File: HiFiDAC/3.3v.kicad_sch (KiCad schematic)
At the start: 7 parts, among them U1 TPS7A90

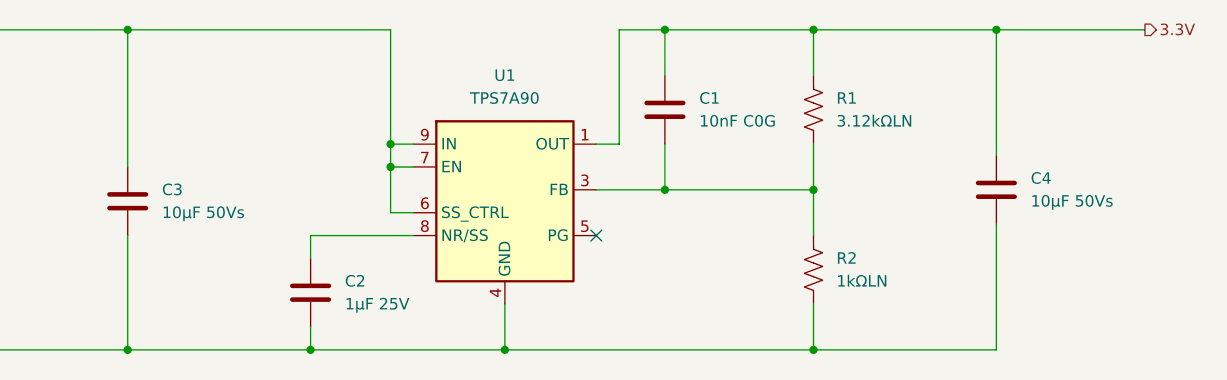
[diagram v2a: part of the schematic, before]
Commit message: HiFiDAC renumbered and footprints assigned
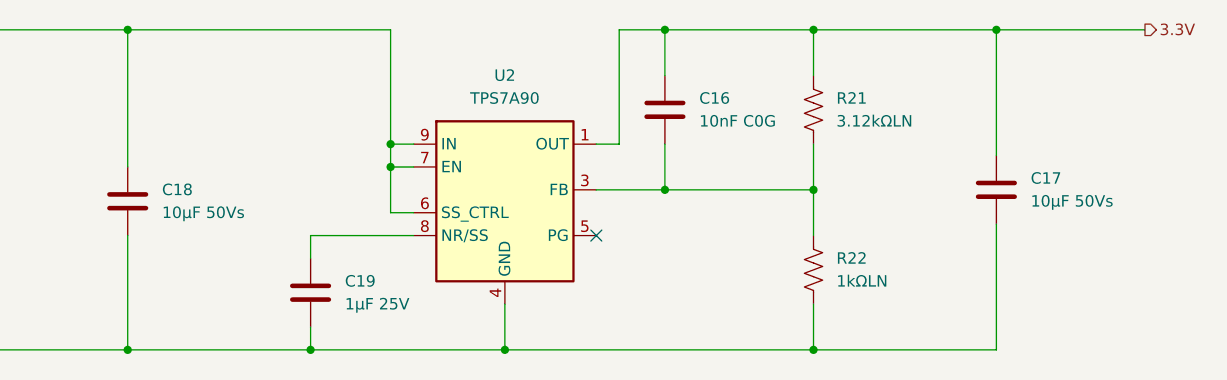
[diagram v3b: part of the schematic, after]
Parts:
- C16: renamed from C1; footprint (none) -> Capacitor_SMD:C_0603_1608Metric
- C17: renamed from C4; footprint (none) -> Capacitor_SMD:C_0805_2012Metric
- C18: renamed from C3; footprint (none) -> Capacitor_SMD:C_0805_2012Metric
- C19: renamed from C2; footprint (none) -> Capacitor_SMD:C_0603_1608Metric
- R21: renamed from R1; footprint (none) -> Resistor_SMD:R_0603_1608Metric
- R22: renamed from R2; footprint (none) -> Resistor_SMD:R_0603_1608Metric
- renumbered U1 to U2
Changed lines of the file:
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@@
 		(dnp no)
 		(fields_autoplaced yes)
-		(property "Reference" "R1"
+		(property "Reference" "R21"
 			(at 180.34 88.8999 0)
 			(effects
@@
 			)
 		)
-		(property "Footprint" ""
+		(property "Footprint" "Resistor_SMD:R_0603_1608Metric"
 			(at 178.816 90.424 90)
 			(effects
@@
 			(project ""
 				(path "/9ca5e549-4577-422c-b8f3-d4e6ad408ec3/d2b42ea6-55ff-4972-b433-f15f9f1c7608"
-					(reference "R1")
+					(reference "R21")
 					(unit 1)
 				)
@@
 		(dnp no)
 		(fields_autoplaced yes)
-		(property "Reference" "C3"
+		(property "Reference" "C18"
 			(at 105.41 99.0599 0)
 			(effects
@@
 			)
 		)
-		(property "Footprint" ""
+		(property "Footprint" "Capacitor_SMD:C_0805_2012Metric"
 			(at 102.5652 104.14 0)
 			(effects
@@
 			(project "HiFiDAC"
 				(path "/9ca5e549-4577-422c-b8f3-d4e6ad408ec3/d2b42ea6-55ff-4972-b433-f15f9f1c7608"
-					(reference "C3")
+					(reference "C18")
 					(unit 1)
 				)
@@
 		(dnp no)
 		(fields_autoplaced yes)
-		(property "Reference" "C4"
+		(property "Reference" "C17"
 			(at 201.93 97.7899 0)
 			(effects
@@
 			)
 		)
-		(property "Footprint" ""
+		(property "Footprint" "Capacitor_SMD:C_0805_2012Metric"
 			(at 199.0852 102.87 0)
 			(effects
@@
 			(project "HiFiDAC"
 				(path "/9ca5e549-4577-422c-b8f3-d4e6ad408ec3/d2b42ea6-55ff-4972-b433-f15f9f1c7608"
-					(reference "C4")
+					(reference "C17")
 					(unit 1)
 				)
@@
 		(dnp no)
 		(fields_autoplaced yes)
-		(property "Reference" "R2"
+		(property "Reference" "R22"
 			(at 180.34 106.6799 0)
 			(effects
@@
 			)
 		)
-		(property "Footprint" ""
+		(property "Footprint" "Resistor_SMD:R_0603_1608Metric"
 			(at 178.816 108.204 90)
 			(effects
@@
 			(project "HiFiDAC"
 				(path "/9ca5e549-4577-422c-b8f3-d4e6ad408ec3/d2b42ea6-55ff-4972-b433-f15f9f1c7608"
-					(reference "R2")
+					(reference "R22")
 					(unit 1)
 				)
@@
 		(dnp no)
 		(fields_autoplaced yes)
-		(property "Reference" "C2"
+		(property "Reference" "C19"
 			(at 125.73 109.2199 0)
 			(effects
@@
 			)
 		)
-		(property "Footprint" ""
+		(property "Footprint" "Capacitor_SMD:C_0603_1608Metric"
 			(at 122.8852 114.3 0)
 			(effects
@@
 			(project "HiFiDAC"
 				(path "/9ca5e549-4577-422c-b8f3-d4e6ad408ec3/d2b42ea6-55ff-4972-b433-f15f9f1c7608"
-					(reference "C2")
+					(reference "C19")
 					(unit 1)
 				)
@@
 		(dnp no)
 		(fields_autoplaced yes)
-		(property "Reference" "C1"
+		(property "Reference" "C16"
 			(at 165.1 88.8999 0)
 			(effects
@@
 			)
 		)
-		(property "Footprint" ""
+		(property "Footprint" "Capacitor_SMD:C_0603_1608Metric"
 			(at 162.2552 93.98 0)
 			(effects
@@
 			(project ""
 				(path "/9ca5e549-4577-422c-b8f3-d4e6ad408ec3/d2b42ea6-55ff-4972-b433-f15f9f1c7608"
-					(reference "C1")
+					(reference "C16")
 					(unit 1)
 				)
@@
 		(dnp no)
 		(fields_autoplaced yes)
-		(property "Reference" "U1"
+		(property "Reference" "U2"
 			(at 143.51 86.36 0)
 			(effects
@@
 			(project ""
 				(path "/9ca5e549-4577-422c-b8f3-d4e6ad408ec3/d2b42ea6-55ff-4972-b433-f15f9f1c7608"
-					(reference "U1")
-					(unit 1)
-				)
+					(reference "U2")
+					(unit 1)
+				)

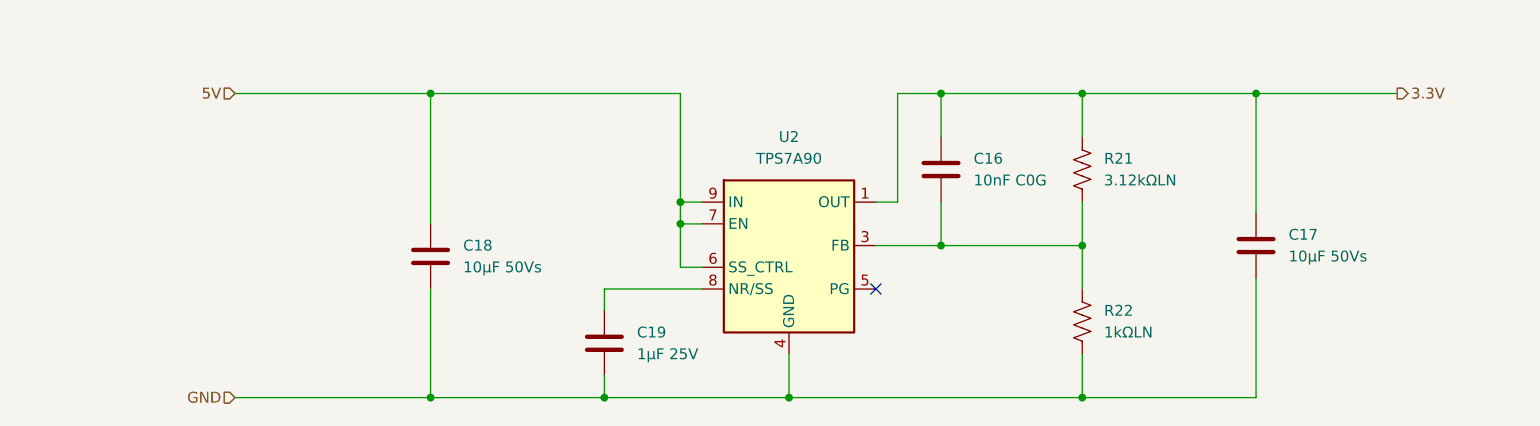
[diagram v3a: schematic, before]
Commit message: HiFiDAC redesign of clocking, digital IO, ferrite beads
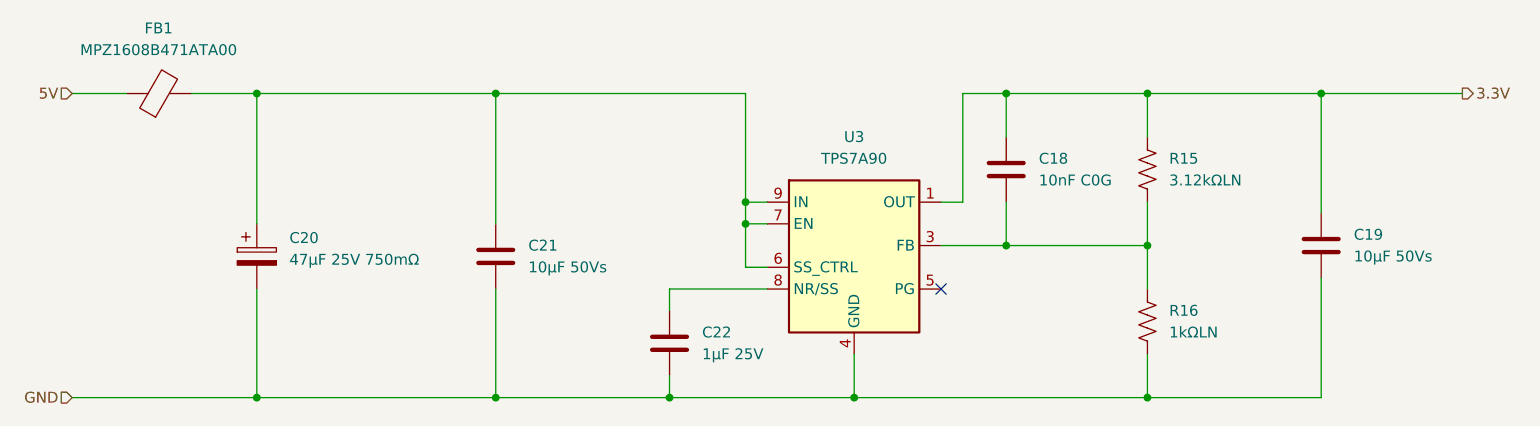
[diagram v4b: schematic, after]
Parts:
- added C20: 47µF 25V 750mΩ, Capacitor_SMD:CP_Elec_6.3x7.7, symbol Device:C_Polarized
- added FB1: MPZ1608B471ATA00, Inductor_SMD:L_0603_1608Metric, symbol Device:FerriteBead
- renumbered C16 to C18, C17 to C19, C18 to C21, C19 to C22, R21 to R15, R22 to R16, U2 to U3
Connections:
- net 5V: now also FB1.1; no longer C21.1, U3.10 (IN), U3.6 (SS_CTRL), U3.7 (EN), U3.9 (IN)
- net GND: now also C20.2
- new net: C20.1, C21.1, FB1.2, U3.10 (IN), U3.6 (SS_CTRL), U3.7 (EN), U3.9 (IN)
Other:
- moved on the sheet: C18, C19, C21, C22, R15, R16, U3

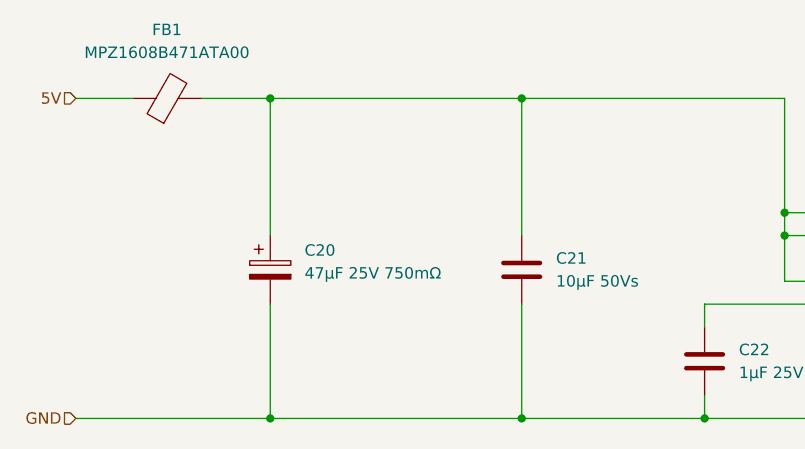
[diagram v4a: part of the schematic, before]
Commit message: HiFiDAC initial layout complete
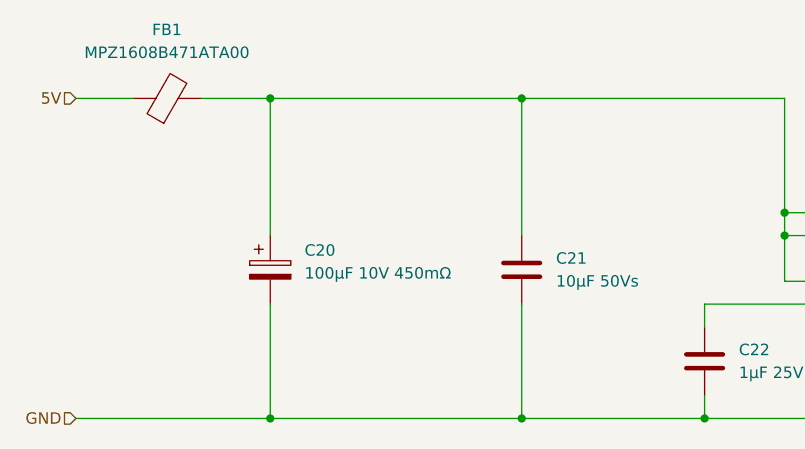
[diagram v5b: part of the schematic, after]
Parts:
- C20: value 47µF 25V 750mΩ -> 100µF 10V 450mΩ
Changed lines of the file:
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@@
 			)
 		)
-		(property "Value" "47µF 25V 750mΩ"
+		(property "Value" "100µF 10V 450mΩ"
 			(at 85.09 100.7109 0)
 			(effects

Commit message: HiFiDAC v2 progress
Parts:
- removed FB1: MPZ1608B471ATA00, Inductor_SMD:L_0603_1608Metric, symbol Device:FerriteBead
- removed U3: TPS7A90, Package_DFN_QFN:Texas_S-PDSO-N10_EP1.2x2mm, symbol Regulator_Linear:TPS7A90
- added C1, C40, C8: 100µF 6.3V, symbol Device:C_Polarized
- added C10, C11, C38, C39: 10µF 25V, Capacitor_SMD:C_0603_1608Metric, symbol Device:C
- added C15, C37, C5: 0.1µF, Capacitor_SMD:C_0603_1608Metric, symbol Device:C
- added C6, C7: 10µF 50Vs, Capacitor_SMD:C_0805_2012Metric, symbol Device:C
- added C9: 1µF 25V, Capacitor_SMD:C_0603_1608Metric, symbol Device:C
- added R1: 3.12kΩLN, Resistor_SMD:R_0603_1608Metric, symbol Device:R_US
- added R2: 1kΩLN, Resistor_SMD:R_0603_1608Metric, symbol Device:R_US
- added R5, R8: 10kΩ, Resistor_SMD:R_0603_1608Metric, symbol Device:R_US
- added R6, R7: 49.9kΩ, Resistor_SMD:R_0603_1608Metric, symbol Device:R_US
- added U2: TPS7A87, Package_DFN_QFN:QFN-20-1EP_4x4mm_P0.5mm_EP2.7x2.7mm, symbol BW_Active:TPS7A87
- added U3: TLV75101, BW_Active:WSON-10-1EP_2x2mm_P0.4mm_EP0.9x1.5mm, symbol BW_Active:TLV75101
- C18: value 10nF C0G -> 0.1µF
- C20: value 100µF 10V 450mΩ -> 100µF 6.3V; footprint Capacitor_SMD:CP_Elec_6.3x7.7 -> (none)
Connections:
- net 5V: now also C21.1, C10.1, C38.1, C6.1, U2.1 (IN), U2.18 (SS_CTRL), U2.2 (IN), U2.20 (EN), U2.4 (IN), U2.5 (IN), U2.6 (EN), U2.8 (SS_CTRL), U3.3 (EN), U3.5 (EN), U3.6 (IN), U3.9 (IN)
- net GND: now also C1.2, C10.2, C11.2, C38.2, C39.2, C40.2, C6.2, C7.2, C8.2, C9.2, R2.2, R5.2, R8.2, U2.13 (GND), U2.21 (EP), U2.3 (GND), U3.11 (EP), U3.2 (GND), U3.4 (GND)
- net at C18.2, R15.2, R16.1: now also U2.16 (FB)
- net 3.3VA: now reaches C20.1
- net 3.3VA: now also C11.1, C15.1, R6.1, U3.10 (OUT); no longer C21.1
- net at C22.1: now also U2.19 (NR/SS)
- net 3.3V renamed 3.3VDAC1
- net 3.3VDAC1: now also C1.1, U2.14 (OUT), U2.15 (OUT)
- new net: C9.1, U2.7 (NR/SS)
- new net: C5.2, R1.2, R2.1, U2.10 (FB)
- new net: C37.2, R7.2, R8.1, U3.7 (FB)
- new net: C15.2, R5.1, R6.2, U3.1 (FB)
- new net 3.3VD: C37.1, C39.1, C40.1, R7.1, U3.8 (OUT)
- new net 3.3VDAC2: C5.1, C7.1, C8.1, R1.1, U2.11 (OUT), U2.12 (OUT)
- no-connect marks 1 -> 2
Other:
- moved on the sheet: C18, C19, C21, C22, R15, R16

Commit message: HiFiDAC v2 progress
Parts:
- C18: renamed from C1; value 100µF 6.3V -> 220µF 6.3V; footprint (none) -> Capacitor_THT:CP_Radial_D5.0mm_P2.00mm
- C23: renamed from C8; value 100µF 6.3V -> 220µF 6.3V; footprint (none) -> Capacitor_THT:CP_Radial_D5.0mm_P2.00mm
- C26: renamed from C10; footprint Capacitor_SMD:C_0603_1608Metric -> Capacitor_SMD:C_0805_2012Metric
- C27: renamed from C11; footprint Capacitor_SMD:C_0603_1608Metric -> Capacitor_SMD:C_0805_2012Metric
- C28: renamed from C20; value 100µF 6.3V -> 100µF 10V; footprint (none) -> Capacitor_THT:CP_Radial_D6.3mm_P2.50mm
- C30: renamed from C38; footprint Capacitor_SMD:C_0603_1608Metric -> Capacitor_SMD:C_0805_2012Metric
- C31: renamed from C39; footprint Capacitor_SMD:C_0603_1608Metric -> Capacitor_SMD:C_0805_2012Metric
- C32: renamed from C40; value 100µF 6.3V -> 100µF 10V 450mΩ; footprint (none) -> Capacitor_SMD:CP_Elec_6.3x7.7
- renumbered C18 to C15, C21 to C16, C19 to C17, C22 to C19, C5 to C20, C6 to C21, C7 to C22, C9 to C24, C15 to C25, C37 to C29, R2 to R10, R6 to R11, R5 to R12, R7 to R13, R8 to R14, R15 to R7, R16 to R8, R1 to R9, U2 to U4, U3 to U5
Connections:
- net 3.3VDAC1: now also U4.11 (OUT), U4.12 (OUT); no longer U4.14 (OUT), U4.15 (OUT)
- net 3.3VDAC2: now also U4.14 (OUT), U4.15 (OUT); no longer U4.11 (OUT), U4.12 (OUT)
- net at C24.1: now also U4.19 (NR/SS); no longer U4.7 (NR/SS)
- net at C15.2, R7.2, R8.1: now also U4.10 (FB); no longer U4.16 (FB)
- net at C20.2, R10.1, R9.2: now also U4.16 (FB); no longer U4.10 (FB)
- net at C19.1: now also U4.7 (NR/SS); no longer U4.19 (NR/SS)
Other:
- moved on the sheet: U4A, U4B

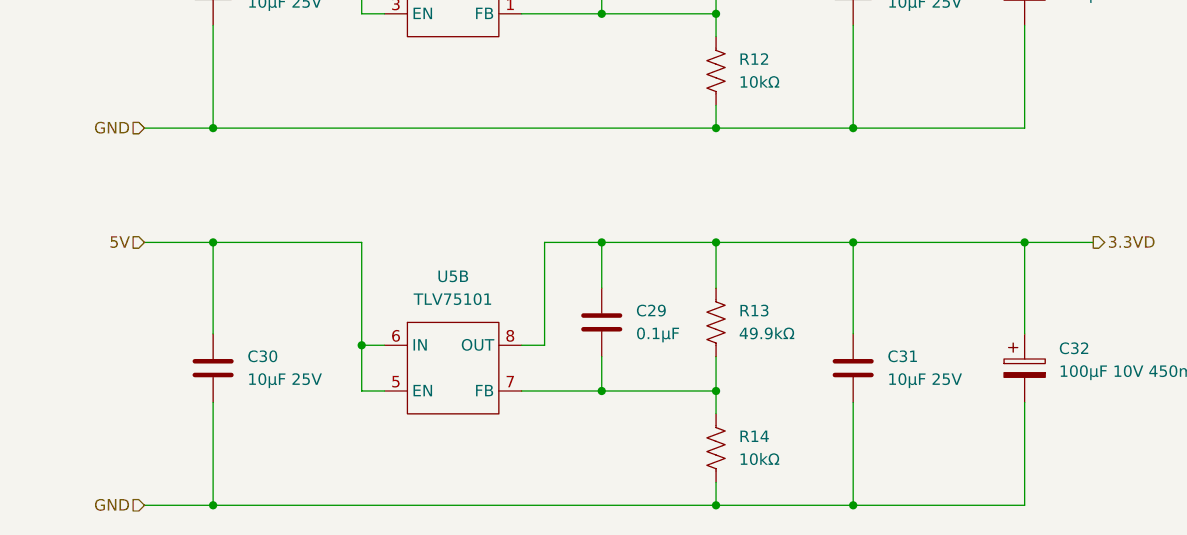
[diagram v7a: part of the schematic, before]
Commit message: HiFiDAC v2 layout+route progress
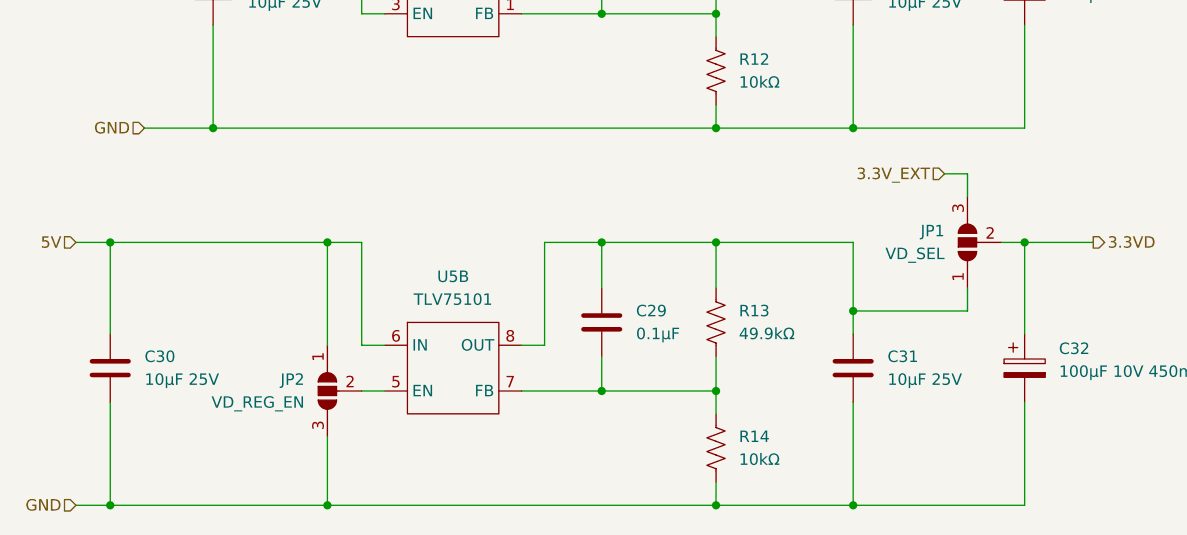
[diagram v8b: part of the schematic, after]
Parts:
- added JP1: VD_SEL, Jumper:SolderJumper-3_P1.3mm_Open_RoundedPad1.0x1.5mm, symbol Jumper:SolderJumper_3_Open
- added JP2: VD_REG_EN, Jumper:SolderJumper-3_P1.3mm_Open_RoundedPad1.0x1.5mm, symbol Jumper:SolderJumper_3_Open
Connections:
- net 3.3VD: now also JP1.2 (C); no longer C29.1, C31.1, R13.1, U5.8 (OUT)
- net 5V: now also JP2.1 (A); no longer U5.5 (EN)
- net GND: now also JP2.3 (B)
- new net: C29.1, C31.1, JP1.1 (A), R13.1, U5.8 (OUT)
- new net: JP2.2 (C), U5.5 (EN)
- new net 3.3V_EXT: JP1.3 (B)
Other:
- moved on the sheet: C30
